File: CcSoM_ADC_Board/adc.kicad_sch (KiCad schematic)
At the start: 17 parts, among them J13 Conn_02x03_Odd_Even, J14 Conn_02x03_Odd_Even, J15 Conn_02x02_Counter_Clockwise

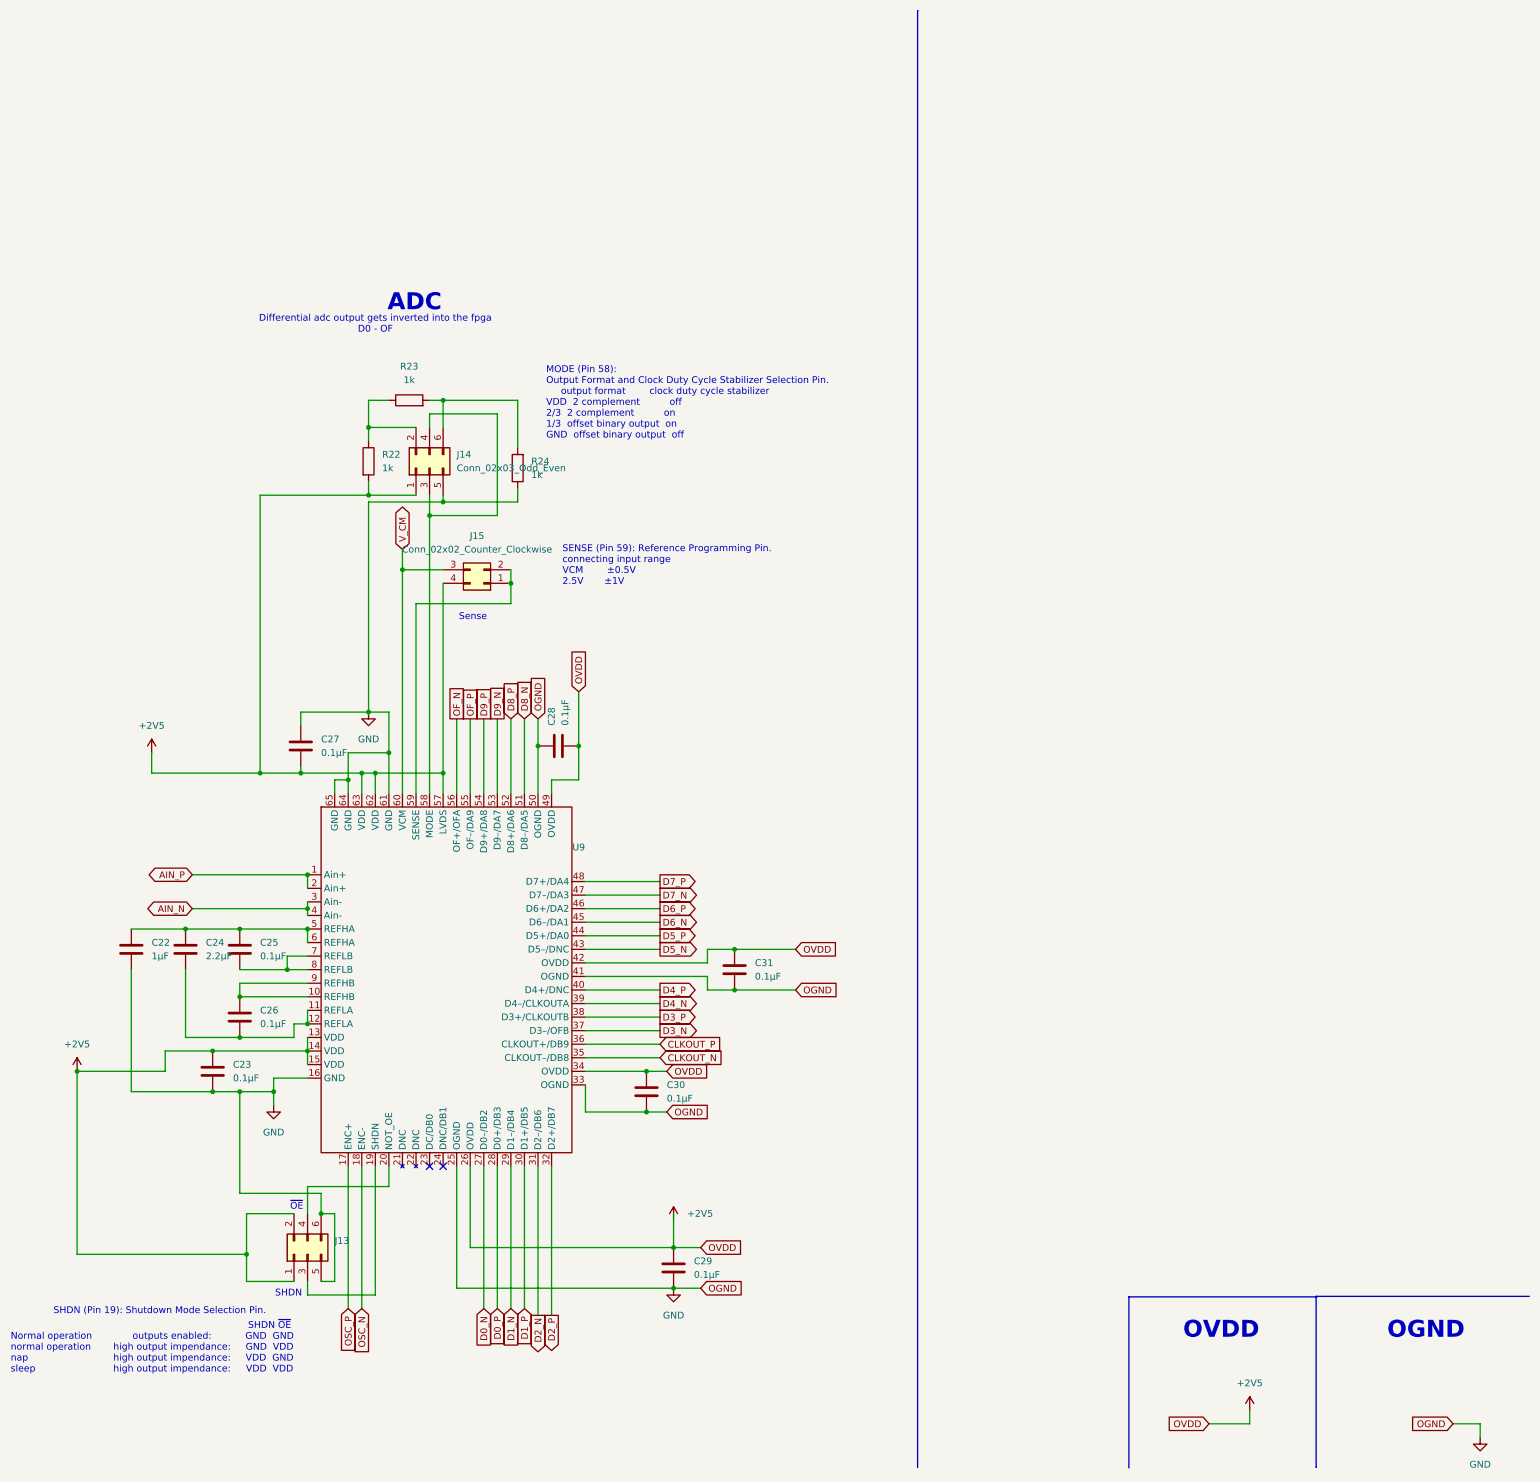
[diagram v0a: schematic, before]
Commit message: changed from 10Bit ADC to 12Bit
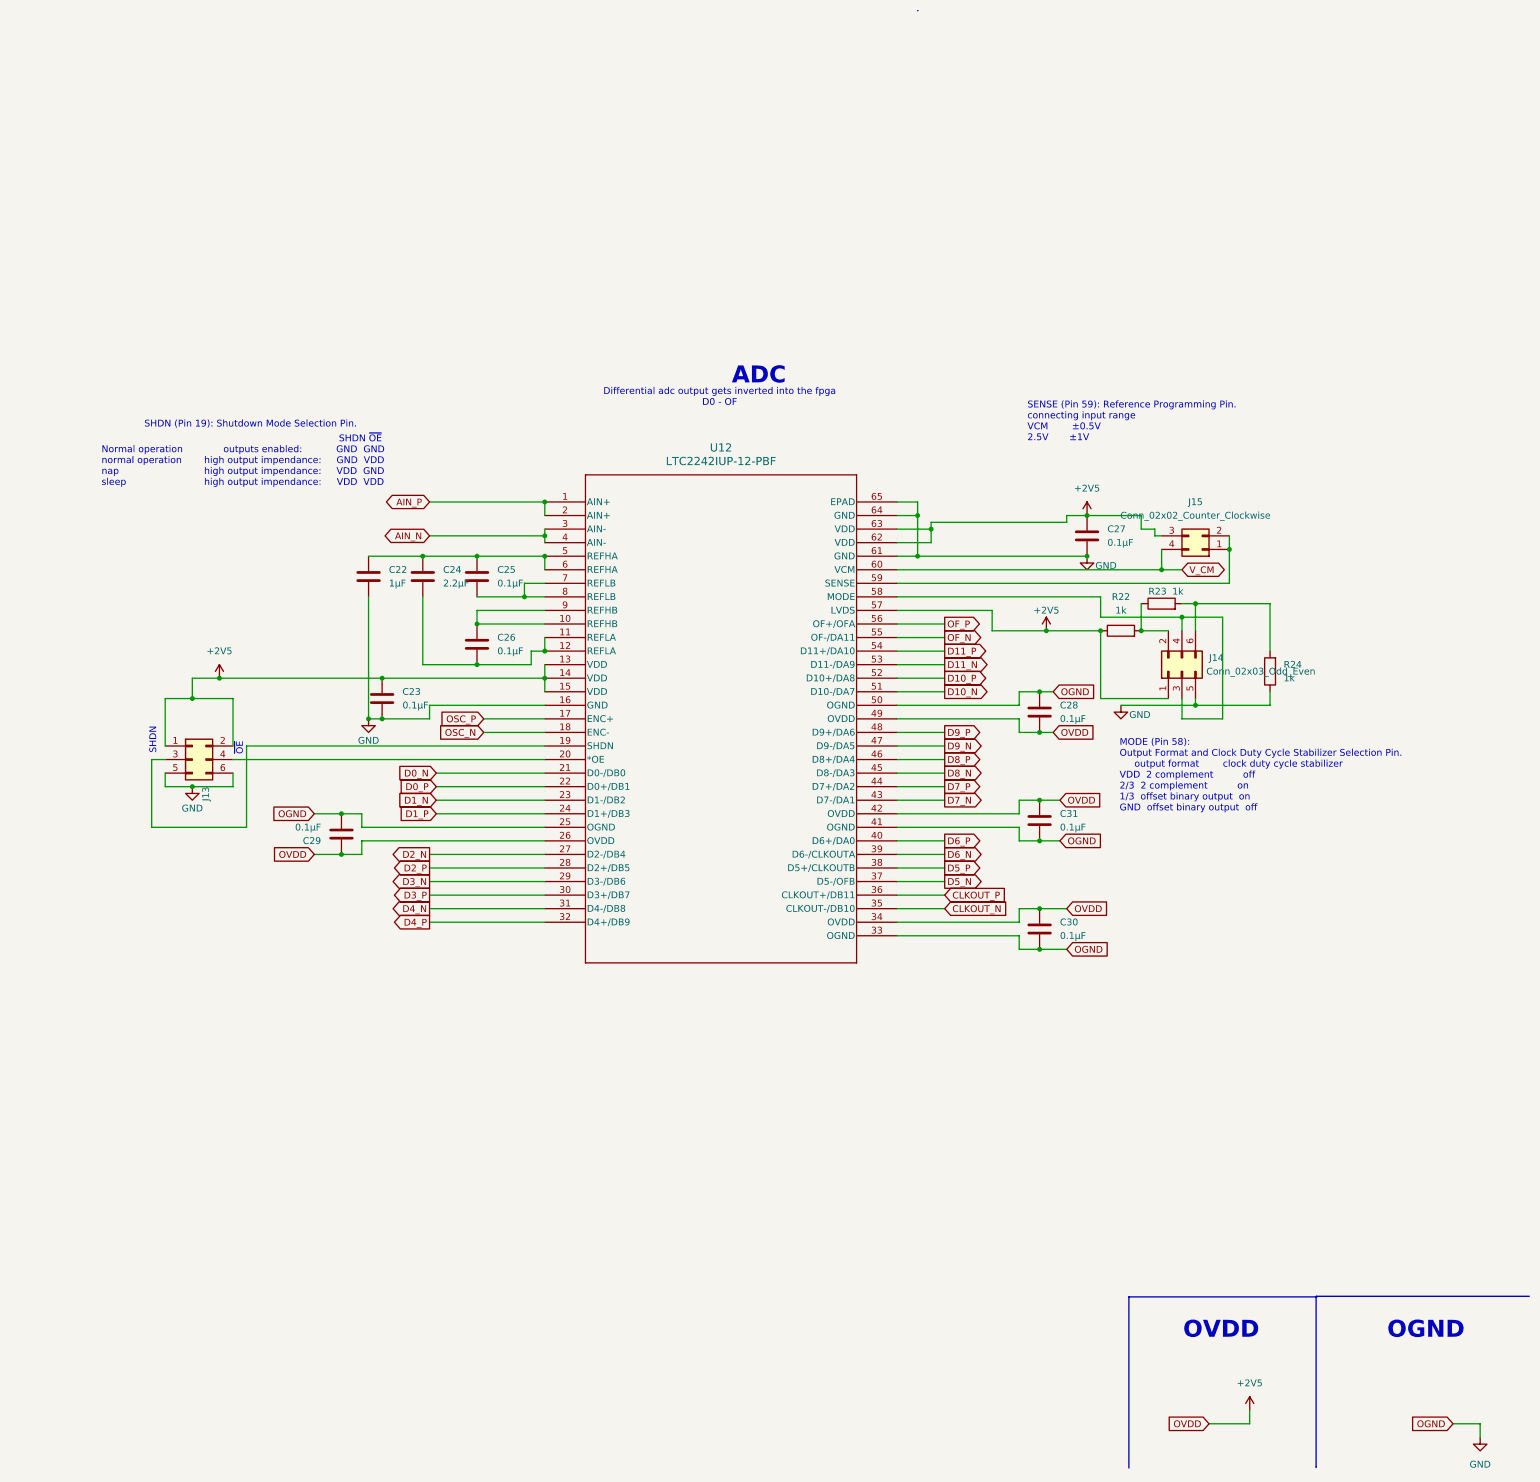
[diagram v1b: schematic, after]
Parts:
- removed U9: ~, Package_DFN_QFN:QFN-64-1EP_9x9mm_P0.5mm_EP7.15x7.15mm, symbol test:LTC2242-10
- added U12: LTC2242IUP-12-PBF, LTC2242-12:QFN-64_UP_LIT, symbol LTC2242-12:LTC2242IUP-12-PBF
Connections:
- net +2V5: now also J15.3 (Pin_3), R22.1, U12.13 (VDD), U12.14 (VDD), U12.15 (VDD), U12.26 (OVDD), U12.34 (OVDD), U12.42 (OVDD), U12.49 (OVDD), U12.57 (LVDS), U12.62 (VDD), U12.63 (VDD); no longer J15.4 (Pin_4), R22.2
- net AIN_N: now also U12.3 (AIN-), U12.4 (AIN-)
- net AIN_P: now also U12.1 (AIN+), U12.2 (AIN+)
- net CLKOUT_N: now also U12.35 (CLKOUT-/DB10)
- net CLKOUT_P: now also U12.36 (CLKOUT+/DB11)
- net D0_N: now also U12.21 (D0-/DB0)
- net D0_P: now also U12.22 (D0+/DB1)
- net D1_N: now also U12.23 (D1-/DB2)
- net D1_P: now also U12.24 (D1+/DB3)
- net D2_N: now also U12.27 (D2-/DB4)
- net D2_P: now also U12.28 (D2+/DB5)
- net D3_N: now also U12.29 (D3-/DB6)
- net D3_P: now also U12.30 (D3+/DB7)
- net D4_N: now also U12.31 (D4-/DB8)
- net D4_P: now also U12.32 (D4+/DB9)
- net D5_N: now also U12.37 (D5-/OFB)
- net D5_P: now also U12.38 (D5+/CLKOUTB)
- net D6_N: now also U12.39 (D6-/CLKOUTA)
- net D6_P: now also U12.40 (D6+/DA0)
- net D7_N: now also U12.43 (D7-/DA1)
- net D7_P: now also U12.44 (D7+/DA2)
- net D8_N: now also U12.45 (D8-/DA3)
- net D8_P: now also U12.46 (D8+/DA4)
- net D9_N: now also U12.47 (D9-/DA5)
- net D9_P: now also U12.48 (D9+/DA6)
- net GND: now also U12.16 (GND), U12.25 (OGND), U12.33 (OGND), U12.41 (OGND), U12.50 (OGND), U12.61 (GND), U12.64 (GND), U12.65 (EPAD)
- net OF_N: now also U12.55 (OF-/DA11)
- net OF_P: now also U12.56 (OF+/OFA)
- net OSC_N: now also U12.18 (ENC-)
- net OSC_P: now also U12.17 (ENC+)
- net V_CM: now also J15.4 (Pin_4), U12.60 (VCM); no longer J15.3 (Pin_3)
- net at J14.2 (Pin_2), R23.1: now also R22.2; no longer R22.1
- net at C22.1, C24.1, C25.1: now also U12.5 (REFHA), U12.6 (REFHA)
- net at C24.2, C26.2: now also U12.11 (REFLA), U12.12 (REFLA)
- net at C26.1: now also U12.10 (REFHB), U12.9 (REFHB)
- net at J13.3 (Pin_3): now also U12.19 (SHDN)
- net at J13.4 (Pin_4): now also U12.20 (*OE)
- net at J14.3 (Pin_3), J14.4 (Pin_4): now also U12.58 (MODE)
- net at J15.1 (Pin_1), J15.2 (Pin_2): now also U12.59 (SENSE)
- net at C25.2: now also U12.7 (REFLB), U12.8 (REFLB)
- new net D10_N: U12.51 (D10-/DA7)
- new net D10_P: U12.52 (D10+/DA8)
- new net D11_N: U12.53 (D11-/DA9)
- new net D11_P: U12.54 (D11+/DA10)
- no-connect marks 2 -> 0
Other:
- note removed: "Sense"

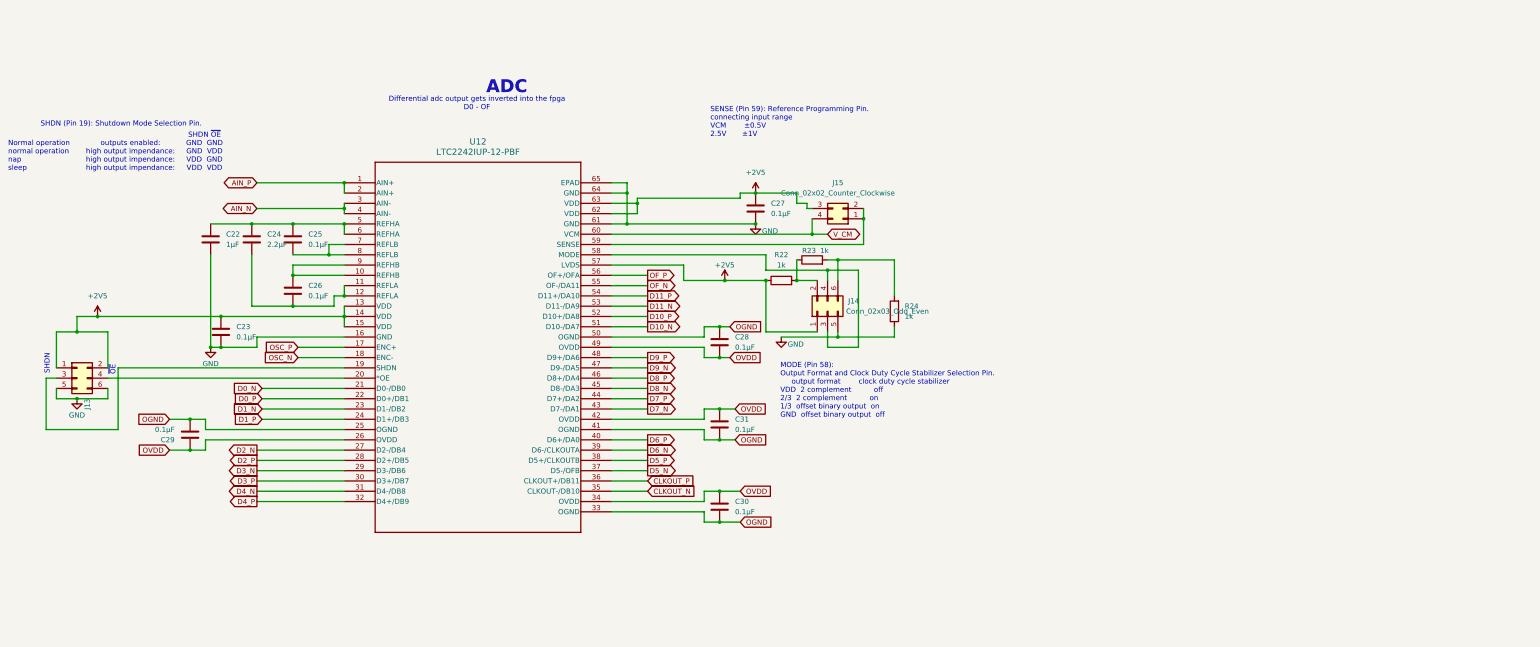
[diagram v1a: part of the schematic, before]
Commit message: corrected schematic created pdf and bom file
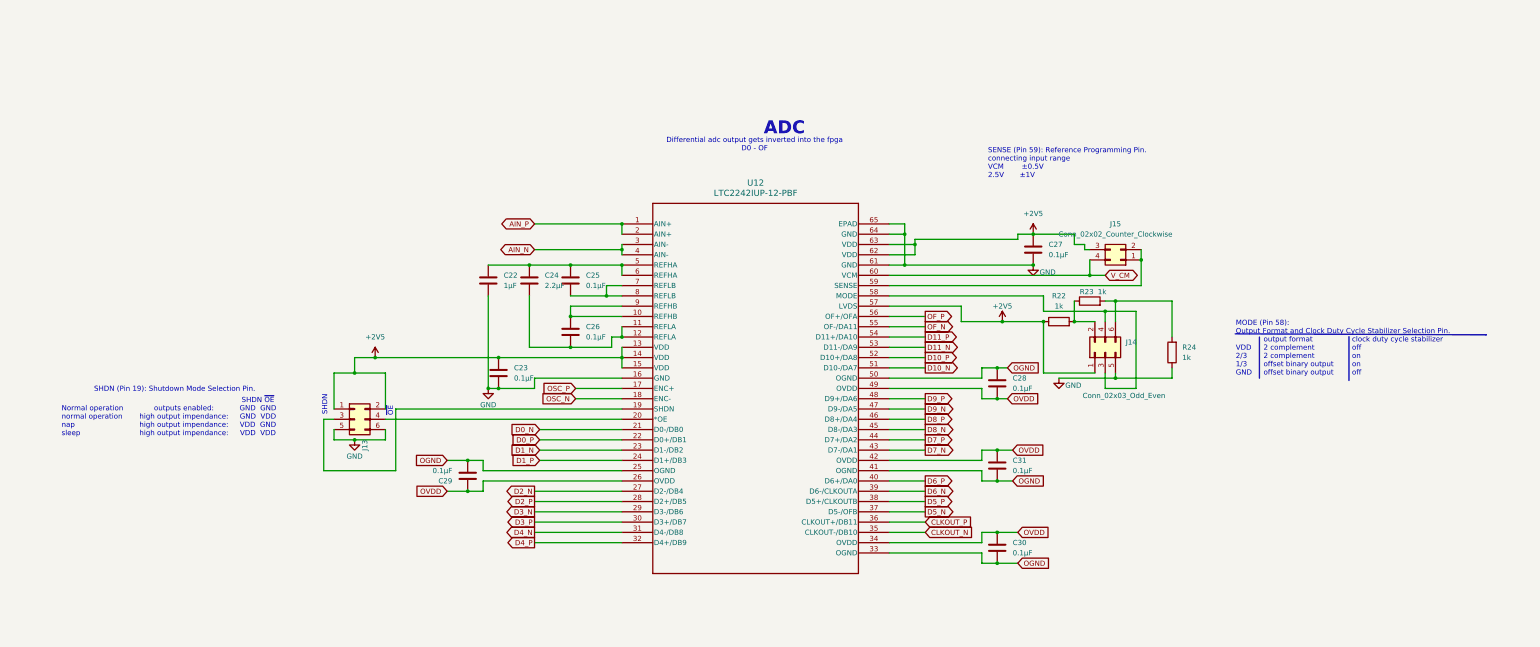
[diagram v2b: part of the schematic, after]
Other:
- note added: "MODE (Pin 58): Output Format and Clock Duty Cycle Stabilizer Selection Pin. VDD 2/3 1/3 GND"
- note added: "clock duty cycle stabilizer off on on off"
- note added: "output format 2 complement 2 complement offset binary output offset binary output"
- note removed: "MODE (Pin 58): Output Format and Clock Duty Cycle Stabilizer Selection Pin. output format clock duty cycle stabilizer VDD 2 complement off 2/3 2 complement on 1/3 offset binary output on GND offset binary output off"
- company: (none) -> Technische Hochschule Köln
- title: (none) -> SoM Programmer & ADC Board
- moved on the sheet: C22, C23, C24, C25, C26, C27, C28, C29, C30, C31, J13, J14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

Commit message: changed schottky, began to add digikey part numbers
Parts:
- U12: DigiKey_no (none) -> LTC2242IUP-12#PBF-ND
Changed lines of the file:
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@@
+			)
+		)
+		(property "DigiKey_no" "LTC2242IUP-12#PBF-ND"
+			(at 184.15 114.3 0)
+			(effects
+				(font
+					(size 1.27 1.27)
+				)
+				(hide yes)
 			)
 		)

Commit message: digikey no not complete
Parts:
- C22: DigiKey_no (none) -> 399-C0603C105K4RACTUCT-ND
- C23, C25, C26, C27, C28, C29, C30, C31: DigiKey_no (none) -> 399-C0603X103J4HACAUTOCT-ND
- C24: DigiKey_no (none) -> 1276-1040-1-ND
- J13, J14: DigiKey_no (none) -> 609-3487-1-ND
- J15: DigiKey_no (none) -> 609-4463-1-ND
- R22, R23, R24: DigiKey_no (none) -> 541-1.00KHCT-ND
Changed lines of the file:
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@@
+			)
+		)
+		(property "DigiKey_no" "399-C0603X103J4HACAUTOCT-ND"
+			(at 146.05 176.53 0)
+			(effects
+				(font
+					(size 1.27 1.27)
+				)
+				(hide yes)
 			)
 		)
@@
 			)
 		)
+		(property "DigiKey_no" "399-C0603X103J4HACAUTOCT-ND"
+			(at 171.45 140.97 0)
+			(effects
+				(font
+					(size 1.27 1.27)
+				)
+				(hide yes)
+			)
+		)
 		(pin "2"
 		)
@@
 			)
 		)
+		(property "DigiKey_no" "399-C0603X103J4HACAUTOCT-ND"
+			(at 285.75 120.65 0)
+			(effects
+				(font
+					(size 1.27 1.27)
+				)
+				(hide yes)
+			)
+		)
 		(pin "2"
 		)
@@
 			)
 		)
+		(property "DigiKey_no" "1276-1040-1-ND"
+			(at 161.29 128.27 0)
+			(effects
+				(font
+					(size 1.27 1.27)
+				)
+				(hide yes)
+			)
+		)
 		(pin "2"
 		)
@@
 		)
 		(property "Description" "Resistor"
+			(at 320.04 146.05 0)
+			(effects
+				(font
+					(size 1.27 1.27)
+				)
+				(hide yes)
+			)
+		)
+		(property "DigiKey_no" "541-1.00KHCT-ND"
 			(at 320.04 146.05 0)
 			(effects
@@
 			)
 		)
+		(property "DigiKey_no" "399-C0603X103J4HACAUTOCT-ND"
+			(at 171.45 128.27 0)
+			(effects
+				(font
+					(size 1.27 1.27)
+				)
+				(hide yes)
+			)
+		)
 		(pin "2"
 		)
@@
 		(property "Description" "Generic connector, double row, 02x03, odd/even pin numbering scheme (row 1 odd numbers, row 2 even numbers), script generated (kicad-library-utils/schlib/autogen/connector/)"
 			(at 303.53 146.05 0)
+			(effects
+				(font
+					(size 1.27 1.27)
+				)
+				(hide yes)
+			)
+		)
+		(property "DigiKey_no" "609-3487-1-ND"
+			(at 303.53 146.05 90)
 			(effects
 				(font
@@
 			)
 		)
+		(property "DigiKey_no" "399-C0603X103J4HACAUTOCT-ND"
+			(at 153.67 151.13 0)
+			(effects
+				(font
+					(size 1.27 1.27)
+				)
+				(hide yes)
+			)
+		)
 		(pin "2"
 		)
@@
 			)
 		)
+		(property "DigiKey_no" "541-1.00KHCT-ND"
+			(at 299.72 133.35 90)
+			(effects
+				(font
+					(size 1.27 1.27)
+				)
+				(hide yes)
+			)
+		)
 		(pin "2"
 		)
@@
 			)
 		)
+		(property "DigiKey_no" "541-1.00KHCT-ND"
+			(at 292.1 138.43 90)
+			(effects
+				(font
+					(size 1.27 1.27)
+				)
+				(hide yes)
+			)
+		)
 		(pin "2"
 		)
@@
 			)
 		)
+		(property "DigiKey_no" "399-C0603C105K4RACTUCT-ND"
+			(at 151.13 128.27 0)
+			(effects
+				(font
+					(size 1.27 1.27)
+				)
+				(hide yes)
+			)
+		)
 		(pin "2"
 		)
@@
 			)
 		)
+		(property "DigiKey_no" "399-C0603X103J4HACAUTOCT-ND"
+			(at 276.86 194.31 0)
+			(effects
+				(font
+					(size 1.27 1.27)
+				)
+				(hide yes)
+			)
+		)
 		(pin "2"
 		)
@@
 			)
 		)
+		(property "DigiKey_no" "609-3487-1-ND"
+			(at 118.11 162.56 90)
+			(effects
+				(font
+					(size 1.27 1.27)
+				)
+				(hide yes)
+			)
+		)
 		(pin "5"
 		)
@@
 			)
 		)
+		(property "DigiKey_no" "399-C0603X103J4HACAUTOCT-ND"
+			(at 276.86 173.99 0)
+			(effects
+				(font
+					(size 1.27 1.27)
+				)
+				(hide yes)
+			)
+		)
 		(pin "2"
 		)
@@
 		)
 		(property "Description" "Unpolarized capacitor"
+			(at 276.86 153.67 0)
+			(effects
+				(font
+					(size 1.27 1.27)
+				)
+				(hide yes)
+			)
+		)
+		(property "DigiKey_no" "399-C0603X103J4HACAUTOCT-ND"
 			(at 276.86 153.67 0)
 			(effects
@@
 			(at 307.34 123.19 0)
 			(effects
+				(font
+					(size 1.27 1.27)
+				)
+				(hide yes)
+			)
+		)
+		(property "DigiKey_no" "609-4463-1-ND"
+			(at 307.34 123.19 0)
+			(effects

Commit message: changed footprint of pinheader from smd to through hole
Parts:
- J13, J14: footprint Connector_PinHeader_2.54mm:PinHeader_2x03_P2.54mm_Vertical_SMD -> Connector_PinHeader_2.54mm:PinHeader_2x03_P2.54mm_Vertical; DigiKey_no 609-3487-1-ND -> 609-3234-ND
- J15: footprint Connector_PinHeader_2.54mm:PinHeader_2x02_P2.54mm_Vertical_SMD -> Connector_PinHeader_2.54mm:PinHeader_2x02_P2.54mm_Vertical; DigiKey_no 609-4463-1-ND -> 609-3233-ND
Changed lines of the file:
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@@
 			)
 		)
-		(property "Footprint" "Connector_PinHeader_2.54mm:PinHeader_2x03_P2.54mm_Vertical_SMD"
+		(property "Footprint" "Connector_PinHeader_2.54mm:PinHeader_2x03_P2.54mm_Vertical"
 			(at 303.53 146.05 0)
 			(effects
@@
 			)
 		)
-		(property "DigiKey_no" "609-3487-1-ND"
+		(property "DigiKey_no" "609-3234-ND"
 			(at 303.53 146.05 90)
 			(effects
@@
 			)
 		)
-		(property "Footprint" "Connector_PinHeader_2.54mm:PinHeader_2x03_P2.54mm_Vertical_SMD"
+		(property "Footprint" "Connector_PinHeader_2.54mm:PinHeader_2x03_P2.54mm_Vertical"
 			(at 118.11 162.56 0)
 			(effects
@@
 			)
 		)
-		(property "DigiKey_no" "609-3487-1-ND"
+		(property "DigiKey_no" "609-3234-ND"
 			(at 118.11 162.56 90)
 			(effects
@@
 			)
 		)
-		(property "Footprint" "Connector_PinHeader_2.54mm:PinHeader_2x02_P2.54mm_Vertical_SMD"
+		(property "Footprint" "Connector_PinHeader_2.54mm:PinHeader_2x02_P2.54mm_Vertical"
 			(at 307.34 123.19 0)
 			(effects
@@
 			)
 		)
-		(property "DigiKey_no" "609-4463-1-ND"
+		(property "DigiKey_no" "609-3233-ND"
 			(at 307.34 123.19 0)
 			(effects
